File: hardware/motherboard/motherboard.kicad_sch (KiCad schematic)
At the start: 37 parts, among them J1 Conn_01x02, J2 Conn_02x03_Odd_Even, J3 Conn_01x04, U1 ESP32-WROOM-32, U2 SHTC3, U3 BMP390, U4 TPS62177DQC

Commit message: Moved hardware files
Moved hadware files to new "motherboard" project and added footprint for the ND005D complete with model.
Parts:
- U5: footprint (none) -> pressureSensorFootprintLibrary:HV120SM02C

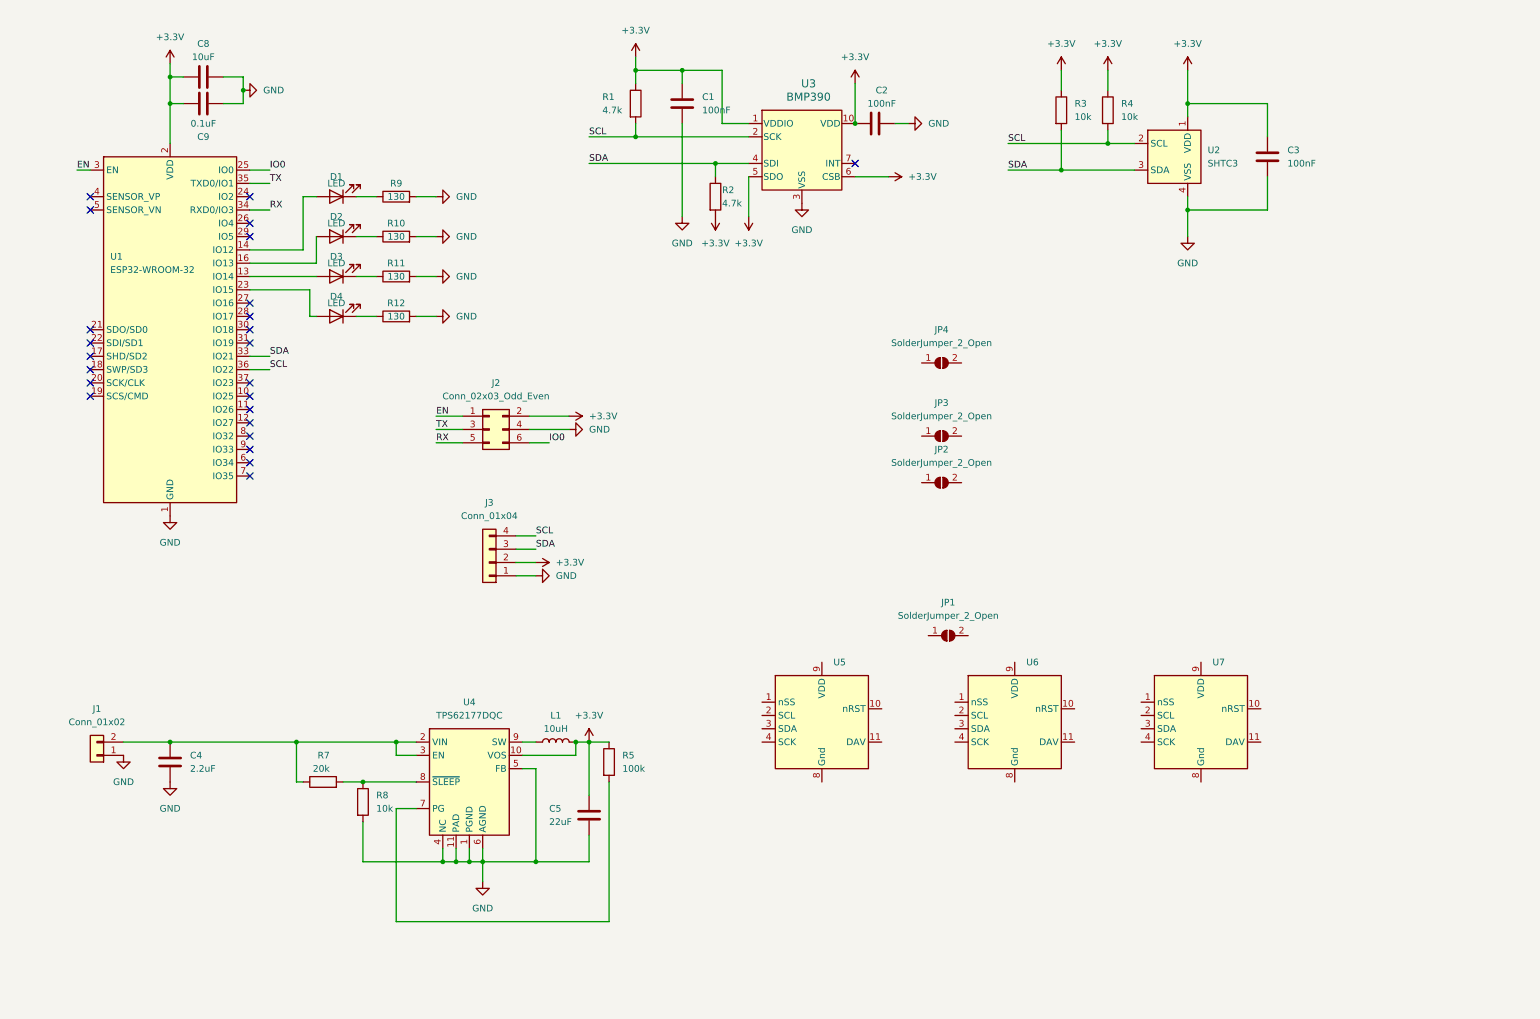
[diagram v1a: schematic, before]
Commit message: Schematic with pressure sensors and transciever
Set up schematic for I2C communication with off board pressure sensors or SPI communication with on board pressure sensors. Added transceiver. Formatted schematic. Added footprints for barometric pressure sensor.
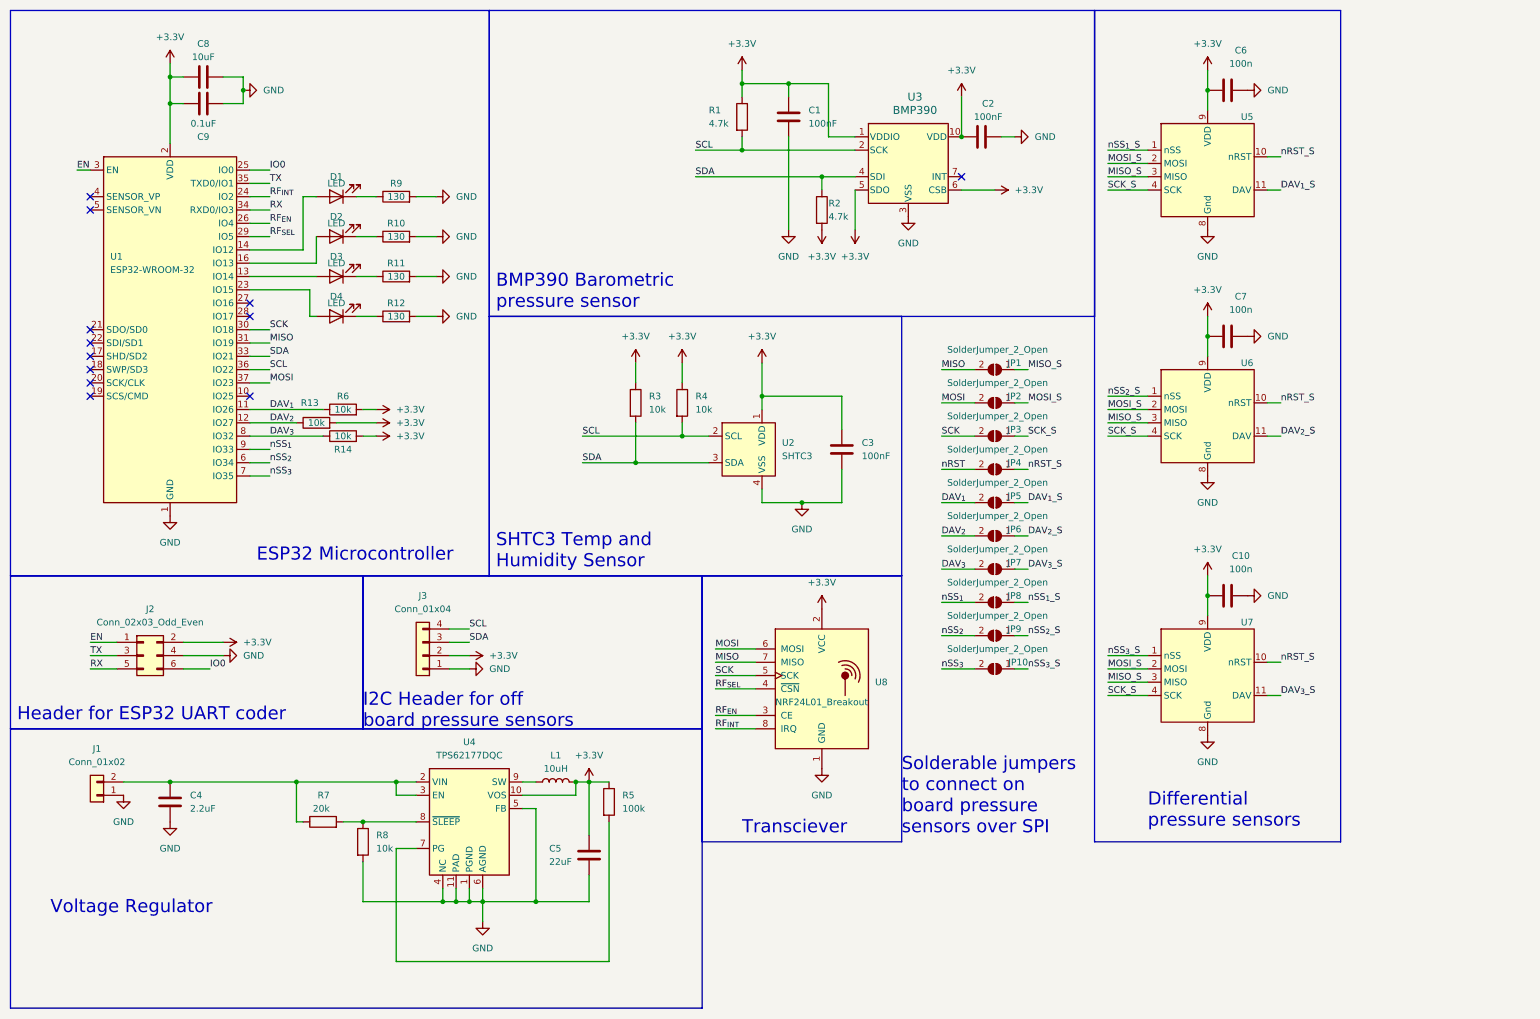
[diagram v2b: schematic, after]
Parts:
- added C10, C6, C7: 100n, symbol Device:C
- added JP10, JP5, JP6, JP7, JP8, JP9: SolderJumper_2_Open, Jumper:SolderJumper-2_P1.3mm_Open_RoundedPad1.0x1.5mm, symbol Jumper:SolderJumper_2_Open
- added R13, R14, R6: 10k, symbol Device:R
- added U8: NRF24L01_Breakout, RF_Module:nRF24L01_Breakout, symbol RF:NRF24L01_Breakout
- JP2, JP3, JP4: footprint Jumper:SolderJumper-2_P1.3mm_Open_Pad1.0x1.5mm -> Jumper:SolderJumper-2_P1.3mm_Open_RoundedPad1.0x1.5mm
- U3: footprint LGA10_BMP390_BOS -> BMP390-footprints:LGA10_BMP390_BOS
- U6, U7: footprint (none) -> pressureSensorFootprintLibrary:HV120SM02C
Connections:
- net +3.3V: now also U5.9 (VDD), U6.9 (VDD), U7.9 (VDD), C10.1, C6.1, C7.1, R13.2, R14.2, R6.2, U8.2 (VCC)
- net GND: now also U5.8 (Gnd), U6.8 (Gnd), U7.8 (Gnd), C10.2, C6.2, C7.2, U8.1 (GND)
- net nSS_{3}_S: now reaches U7.1 (nSS)
- net nSS_{3}_S: now also JP10.1 (A)
- net nRST_S: now reaches U7.10 (nRST)
- net nRST_S: now also JP4.1 (A), U5.10 (nRST), U6.10 (nRST)
- net DAV_{3}_S: now reaches U7.11 (DAV)
- net DAV_{3}_S: now also JP7.1 (A)
- net MOSI_S: now reaches U7.2 (MOSI)
- net MOSI_S: now also JP2.1 (A), U5.2 (MOSI), U6.2 (MOSI)
- net MISO_S: now reaches U7.3 (MISO)
- net MISO_S: now also JP1.1 (A), U5.3 (MISO), U6.3 (MISO)
- net SCK_S: now reaches U7.4 (SCK)
- net SCK_S: now also JP3.1 (A), U5.4 (SCK), U6.4 (SCK)
- net nRST: now reaches JP4.2 (B)
- net nSS_{1}_S: now reaches U5.1 (nSS)
- net nSS_{1}_S: now also JP8.1 (A)
- net DAV_{1}_S: now reaches U5.11 (DAV)
- net DAV_{1}_S: now also JP5.1 (A)
- net MOSI: now reaches JP2.2 (B)
- net MOSI: now also U1.37 (IO23), U8.6 (MOSI)
- net nSS_{2}_S: now reaches U6.1 (nSS)
- net nSS_{2}_S: now also JP9.1 (A)
- net DAV_{2}_S: now reaches U6.11 (DAV)
- net DAV_{2}_S: now also JP6.1 (A)
- net DAV_{1}: now reaches U1.11 (IO26)
- net DAV_{1}: now also JP5.2 (B), R6.1
- net DAV_{2}: now reaches U1.12 (IO27)
- net DAV_{2}: now also JP6.2 (B), R13.1
- net RF_{INT}: now reaches U1.24 (IO2)
- net RF_{INT}: now also U8.8 (IRQ)
- net RF_{EN}: now reaches U1.26 (IO4)
- net RF_{EN}: now also U8.3 (CE)
- net RF_{SEL}: now reaches U1.29 (IO5)
- net RF_{SEL}: now also U8.4 (~{CSN})
- net SCK: now reaches U1.30 (IO18)
- net SCK: now also JP3.2 (B), U8.5 (SCK)
- net MISO: now reaches U1.31 (IO19)
- net MISO: now also JP1.2 (B), U8.7 (MISO)
- net nSS_{2}: now reaches U1.6 (IO34)
- net nSS_{2}: now also JP9.2 (B)
- net nSS_{3}: now reaches U1.7 (IO35)
- net nSS_{3}: now also JP10.2 (B)
- net DAV_{3}: now reaches U1.8 (IO32)
- net DAV_{3}: now also JP7.2 (B), R14.1
- net nSS_{1}: now reaches U1.9 (IO33)
- net nSS_{1}: now also JP8.2 (B)
- no-connect marks 24 -> 12
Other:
- note added: "BMP390 Barometric pressure sensor"
- note added: "Differential pressure sensors"
- note added: "ESP32 Microcontroller"
- note added: "Header for ESP32 UART coder"
- note added: "I2C Header for off board pressure sensors"
- note added: "SHTC3 Temp and Humidity Sensor"
- note added: "Solderable jumpers to connect on board pressure sensors over SPI"
- note added: "Transciever"
- note added: "Voltage Regulator"
- moved on the sheet: C1, C2, C3, C4, C5, J1, J2, J3, JP1, L1, R1, R2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

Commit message: Power solder connections
Added solder connections for power and ground because I forgot them last time and updated footprint assignments
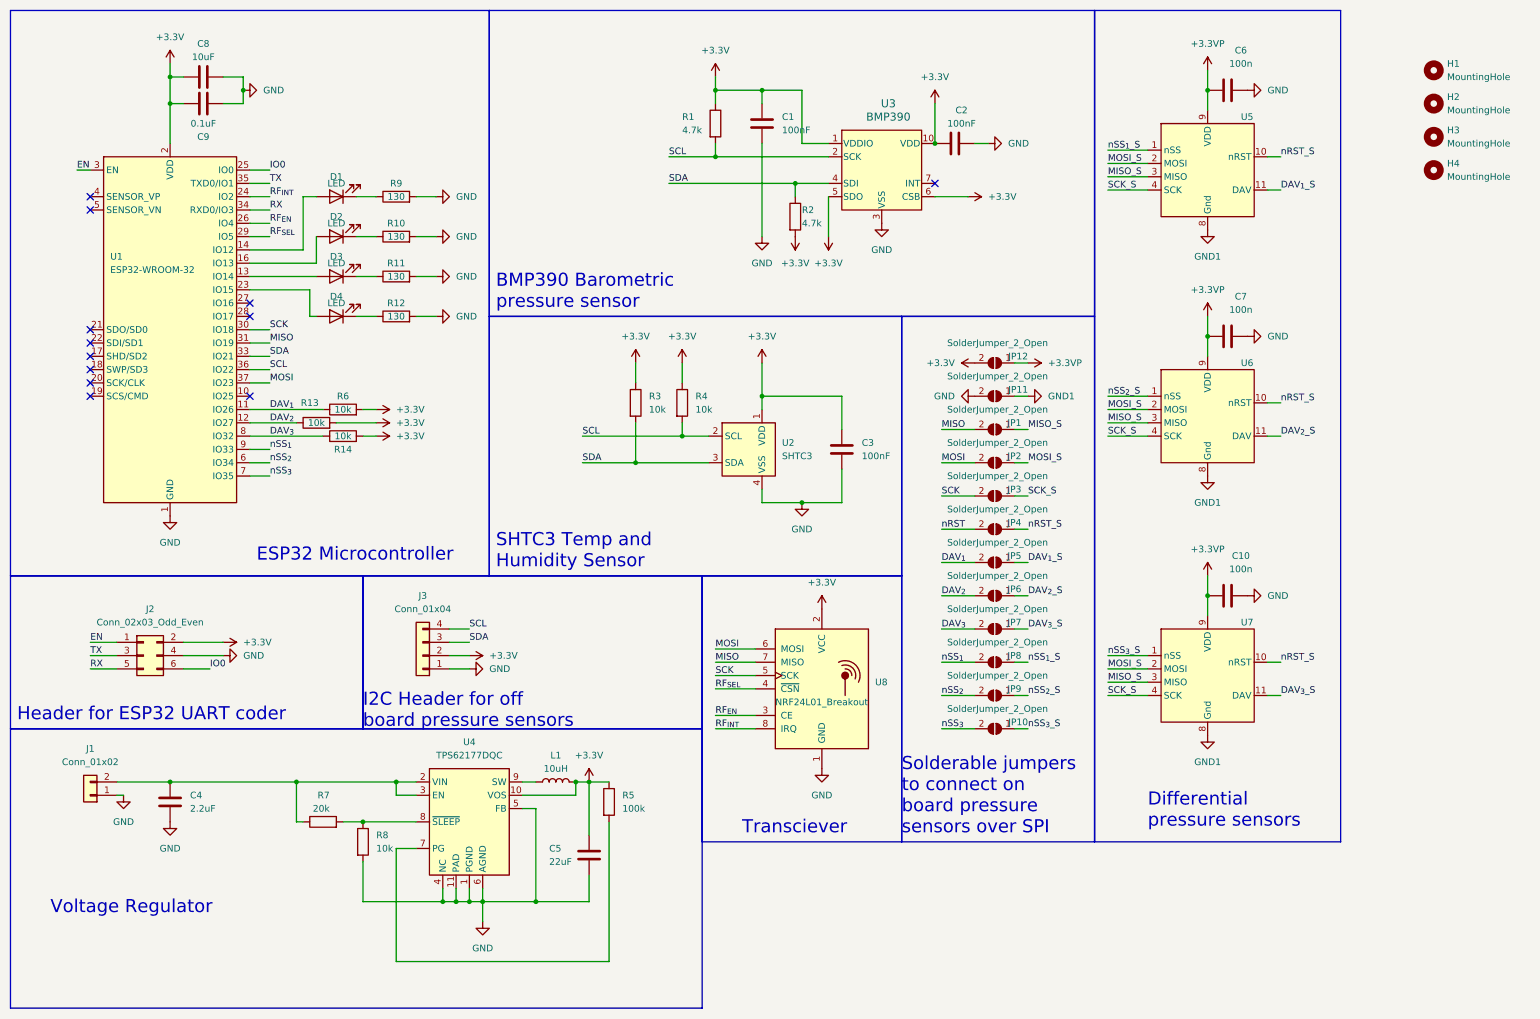
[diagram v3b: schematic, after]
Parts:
- added H1, H2, H3, H4: MountingHole, symbol Mechanical:MountingHole
- added JP11, JP12: SolderJumper_2_Open, Jumper:SolderJumper-2_P1.3mm_Open_RoundedPad1.0x1.5mm, symbol Jumper:SolderJumper_2_Open
- J1: footprint (none) -> Connector_AMASS:AMASS_XT60-F_1x02_P7.20mm_Vertical
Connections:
- net +3.3V: now also JP12.2 (B); no longer C10.1, C6.1, C7.1, U5.9 (VDD), U6.9 (VDD), U7.9 (VDD)
- net GND: now also JP11.2 (B); no longer U5.8 (Gnd), U6.8 (Gnd), U7.8 (Gnd)
- new net +3.3VP: C10.1, C6.1, C7.1, JP12.1 (A), U5.9 (VDD), U6.9 (VDD), U7.9 (VDD)
- new net GND1: JP11.1 (A), U5.8 (Gnd), U6.8 (Gnd), U7.8 (Gnd)
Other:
- moved on the sheet: C1, C2, J1, JP1, JP10, JP2, JP3, JP4, JP5, JP6, JP7, JP8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

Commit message: Completed schematic
Completed schematic with all footprints assigned
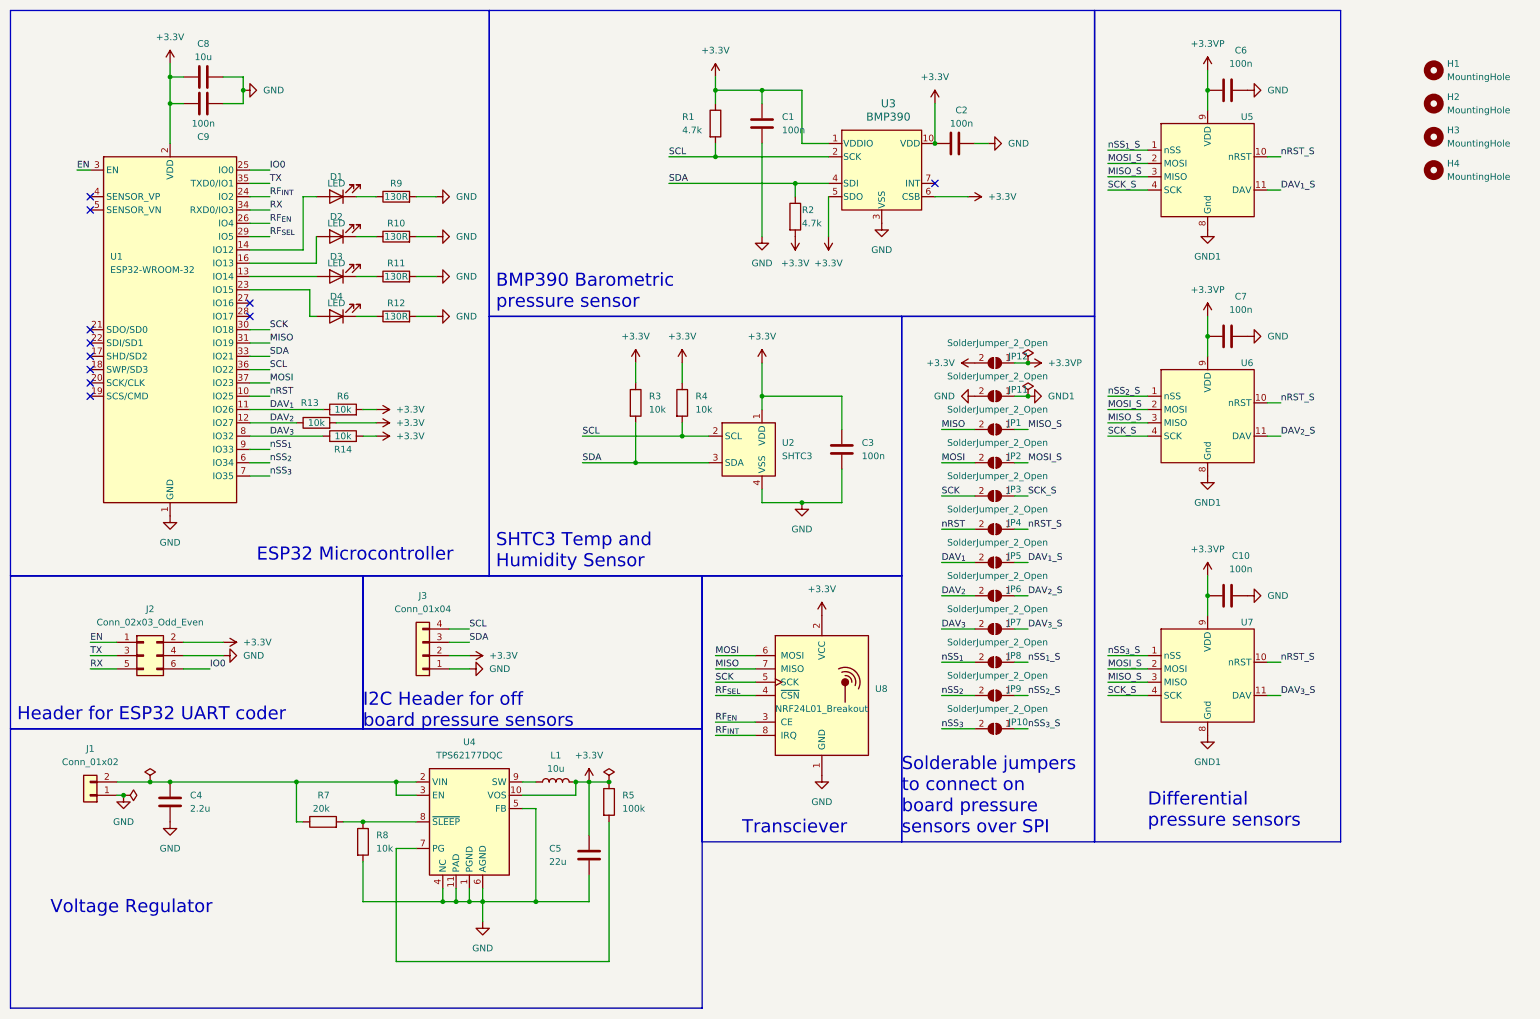
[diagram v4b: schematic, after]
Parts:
- C1, C2, C3: value 100nF -> 100n; footprint (none) -> Capacitor_SMD:C_0603_1608Metric
- C10, C6, C7: footprint (none) -> Capacitor_SMD:C_0603_1608Metric
- C4: value 2.2uF -> 2.2u; footprint (none) -> Capacitor_SMD:C_0603_1608Metric
- C5: value 22uF -> 22u; footprint (none) -> Capacitor_SMD:C_0805_2012Metric
- C8: value 10uF -> 10u; footprint (none) -> Capacitor_SMD:C_0805_2012Metric
- C9: value 0.1uF -> 100n; footprint (none) -> Capacitor_SMD:C_0603_1608Metric
- D1, D2, D3, D4: footprint (none) -> LED_SMD:LED_0805_2012Metric
- H1, H2, H3, H4: footprint (none) -> MountingHole:MountingHole_3mm
- J3: footprint (none) -> Connector_PinSocket_2.54mm:PinSocket_1x04_P2.54mm_Vertical
- L1: value 10uH -> 10u; footprint (none) -> Inductor_SMD:L_Taiyo-Yuden_MD-4040
- R1, R13, R14, R2, R3, R4, R5, R6, R7, R8: footprint (none) -> Resistor_SMD:R_0603_1608Metric
- R10, R11, R12, R9: value 130 -> 130R; footprint (none) -> Resistor_SMD:R_0603_1608Metric
- U3: footprint BMP390-footprints:LGA10_BMP390_BOS -> LGA10_BMP390_BOS
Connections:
- net nRST: now also U1.10 (IO25)
- now unconnected: U5.5 (DNC), U5.6 (DNC), U5.7 (DNC), U6.5 (DNC), U6.6 (DNC), U6.7 (DNC), U7.5 (DNC), U7.6 (DNC), U7.7 (DNC)
- no-connect marks 12 -> 11
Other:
- moved on the sheet: U8
